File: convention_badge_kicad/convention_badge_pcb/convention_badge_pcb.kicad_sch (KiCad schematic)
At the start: 0 parts

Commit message: updated readme and added kicad board reference
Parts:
- added U1: ESP32-C3, Package_DFN_QFN:QFN-32-1EP_5x5mm_P0.5mm_EP3.45x3.45mm, symbol Espressif:ESP32-C3
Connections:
- new net: U1.2 (VDD3P3), U1.3 (VDD3P3)
- new net: U1.31 (VDDA), U1.32 (VDDA)
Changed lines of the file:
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@@
 	(generator_version "9.0")
 	(paper "A4")
+	(symbol
+		(lib_id "Espressif:ESP32-C3")
+		(at 220.98 68.58 0)
+		(unit 1)
+		(exclude_from_sim no)
+		(in_bom yes)
+		(on_board yes)
+		(dnp no)
+		(fields_autoplaced yes)
+		(property "Reference" "U1"
+			(at 223.1233 99.06 0)
+			(effects
+				(font
+					(size 1.27 1.27)
+				)
+				(justify left)
+			)
+		)
+		(property "Value" "ESP32-C3"
+			(at 223.1233 101.6 0)
+			(effects
+				(font
+					(size 1.27 1.27)
+				)
+				(justify left)
+			)
+		)
+		(property "Footprint" "Package_DFN_QFN:QFN-32-1EP_5x5mm_P0.5mm_EP3.45x3.45mm"
+			(at 220.98 106.68 0)
+			(effects
+				(font
+					(size 1.27 1.27)
+				)
+				(hide yes)
+			)
+		)
+		(property "Datasheet" "https://www.espressif.com/sites/default/files/documentation/esp32-c3_datasheet_en.pdf"
+			(at 220.98 109.22 0)
+			(effects
+				(font
+					(size 1.27 1.27)
+				)
+				(hide yes)
+			)
+		)
+		(property "Description" "ESP32-C3 family is an ultra-low-power MCU-based SoC solution that supports 2.4 GHz Wi-Fi and Bluetooth®Low Energy (Bluetooth LE)."
+			(at 220.98 68.58 0)
+			(effects
+				(font
+					(size 1.27 1.27)
+				)
+				(hide yes)
+			)
+		)
+		(pin "9"
+		)
+		(pin "12"
+		)
+		(pin "19"
+		)
+		(pin "4"
+		)
+		(pin "5"
+		)
+		(pin "23"
+		)
+		(pin "1"
+		)
+		(pin "30"
+		)
+		(pin "7"
+		)
+		(pin "29"
+		)
+		(pin "10"
+		)
+		(pin "13"
+		)
+		(pin "18"
+		)
+		(pin "20"
+		)
+		(pin "22"
+		)
+		(pin "31"
+		)
+		(pin "25"
+		)
+		(pin "21"
+		)
+		(pin "6"
+		)
+		(pin "24"
+		)
+		(pin "15"
+		)
+		(pin "2"
+		)
+		(pin "26"
+		)
+		(pin "11"
+		)
+		(pin "33"
+		)
+		(pin "27"
+		)
+		(pin "14"
+		)
+		(pin "16"
+		)
+		(pin "3"
+		)
+		(pin "17"
+		)
+		(pin "8"
+		)
+		(pin "32"
+		)
+		(pin "28"
+		)
+		(instances
+			(project ""
+				(path "/93c09dce-0218-4f0d-87ef-7cd455f2b641"
+					(reference "U1")
+					(unit 1)
+				)
+			)
+		)
+	)
 	(sheet_instances
 		(path "/"

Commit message: v1 schematic and parts list
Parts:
- removed U1: ESP32-C3, Package_DFN_QFN:QFN-32-1EP_5x5mm_P0.5mm_EP3.45x3.45mm, symbol Espressif:ESP32-C3
- added J1: E_Paper_Display, Connector_PinHeader_2.54mm:PinHeader_2x04_P2.54mm_Vertical, symbol Connector_Generic:Conn_02x04_Odd_Even
- added J2: 3.7V Battery, Connector_JST:JST_PH_B2B-PH-K_1x02_P2.00mm_Vertical, symbol Connector_Generic:Conn_01x02
- added JP1, JP2: SolderJumper_2_Open, Jumper:SolderJumper-2_P1.3mm_Open_TrianglePad1.0x1.5mm, symbol Jumper:SolderJumper_2_Open
- added R1, R2: 220k, Resistor_THT:R_Axial_DIN0207_L6.3mm_D2.5mm_P7.62mm_Horizontal, symbol Device:R_US
- added SW1, SW2, SW3: SW_Push, Button_Switch_THT:SW_PUSH_6mm, symbol Switch:SW_Push
- added SW4: SW_SPST, Button_Switch_THT:SW_Slide-03_Wuerth-WS-SLTV_10x2.5x6.4_P2.54mm, symbol Switch:SW_SPST
- added U1: XIAO-ESP32-C3-DIP, XIAO:XIAO-ESP32-C3-DIP, symbol Seeed_Studio_XIAO_Series:XIAO-ESP32-C3-DIP
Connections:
- new net: R2.1, SW4.1 (A)
- new net: JP1.2 (B), R1.2
- new net +3.7V: J2.1 (Pin_1), SW4.2 (B)
- new net ADC: R1.1, R2.2, U1.1 (GPIO2_A0_D0)
- new net BUSY: J1.8 (Pin_8), U1.8 (GPIO20_D7_RX)
- new net BUT_1: SW1.1, U1.2 (GPIO3_A1_D1)
- new net BUT_2: SW2.1, U1.3 (GPIO4_A2_D2)
- new net BUT_3: SW3.1, U1.4 (GPIO5_A3_D3)
- new net CS: J1.5 (Pin_5), U1.6 (GPIO7_D5_SCL)
- new net DC: J1.6 (Pin_6), U1.5 (GPIO6_D4_SDA)
- new net GND: J1.2 (Pin_2), J2.2 (Pin_2), JP2.2 (B), SW1.2, SW2.2, SW3.2, U1.13 (GND)
- new net RET: J1.7 (Pin_7), U1.7 (GPIO21_D6_TX)
- new net SCL: J1.4 (Pin_4), U1.9 (GPIO8_D8_SCK)
- new net SDA: J1.3 (Pin_3), U1.11 (GPIO10_D10_MOSI)
- new net VDD: J1.1 (Pin_1), U1.12 (3V3)
- no-connect marks 0 -> 4

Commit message: created footprint for display and made a (very) rough layout of the board
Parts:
- J1: footprint Connector_PinHeader_2.54mm:PinHeader_2x04_P2.54mm_Vertical -> 2_Displays:2.9_e_paper_ER-EPD029-2-5073
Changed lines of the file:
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@@
 			)
 		)
-		(property "Footprint" "Connector_PinHeader_2.54mm:PinHeader_2x04_P2.54mm_Vertical"
+		(property "Footprint" "2_Displays:2.9_e_paper_ER-EPD029-2-5073"
 			(at 152.4 62.23 0)
 			(effects

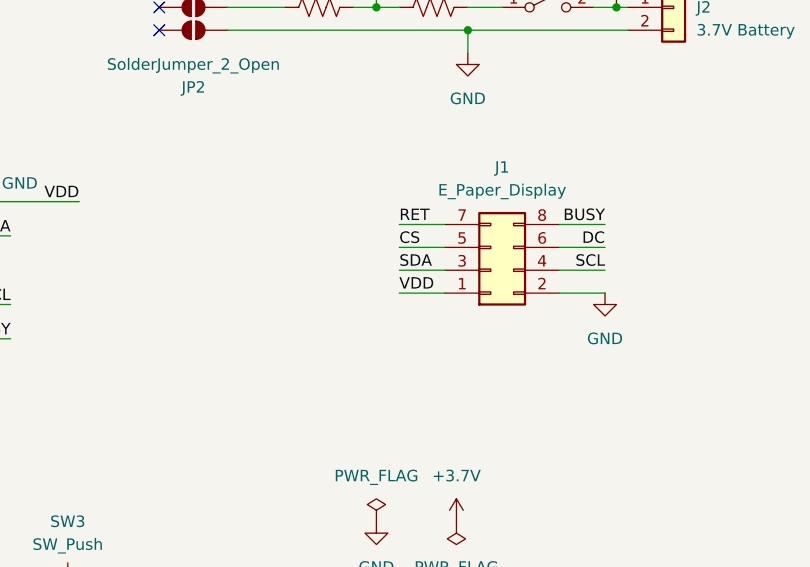
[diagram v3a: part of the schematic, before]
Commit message: finished v1 layout, will serve as backup for if v2 is unfeasable
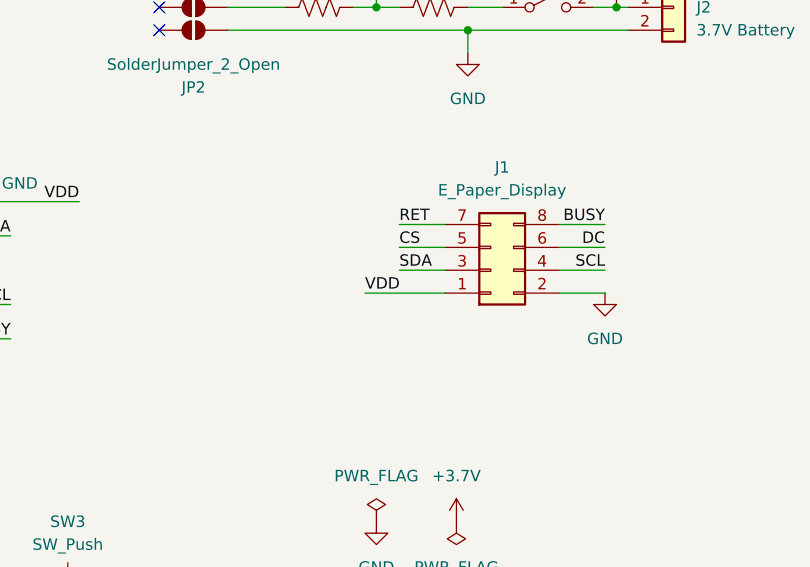
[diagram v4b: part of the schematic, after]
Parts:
- J2: footprint Connector_JST:JST_PH_B2B-PH-K_1x02_P2.00mm_Vertical -> Connector_JST:JST_PH_S2B-PH-K_1x02_P2.00mm_Horizontal
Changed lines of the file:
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@@
+	(wire
+		(pts
+			(xy 138.43 64.77) (xy 147.32 64.77)
+		)
+		(stroke
+			(width 0)
+			(type default)
+		)
+	)
 	(wire
 		(pts
 			(xy 93.98 54.61) (xy 106.68 54.61)
-		)
-		(stroke
-			(width 0)
-			(type default)
-		)
-	)
-	(wire
-		(pts
-			(xy 142.24 64.77) (xy 147.32 64.77)
 		)
 		(stroke
@@
 	)
 	(label "VDD"
-		(at 142.24 64.77 0)
+		(at 138.43 64.77 0)
 		(effects
 			(font
@@
 			)
 		)
-		(property "Footprint" "Connector_JST:JST_PH_B2B-PH-K_1x02_P2.00mm_Vertical"
+		(property "Footprint" "Connector_JST:JST_PH_S2B-PH-K_1x02_P2.00mm_Horizontal"
 			(at 172.72 33.02 0)
 			(effects
